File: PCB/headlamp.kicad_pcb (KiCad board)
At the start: 2 copper layers, 50 x 38 mm, 54 parts, among them J1 USB_B_Mini, J2 Conn_02x03_Odd_Even, Q1 Q_NPN_BCE, Q2 Q_NPN_BCE, Q3 Q_NPN_BCE, Q4 Q_NPN_BCE, SW1 SW_Push, SW2 SW_Push, SW3 SW_Push, SW4 SW_Push, U1 TP4056, U2 ATtiny13A-SS, X1 BATT+, X2 BATT-

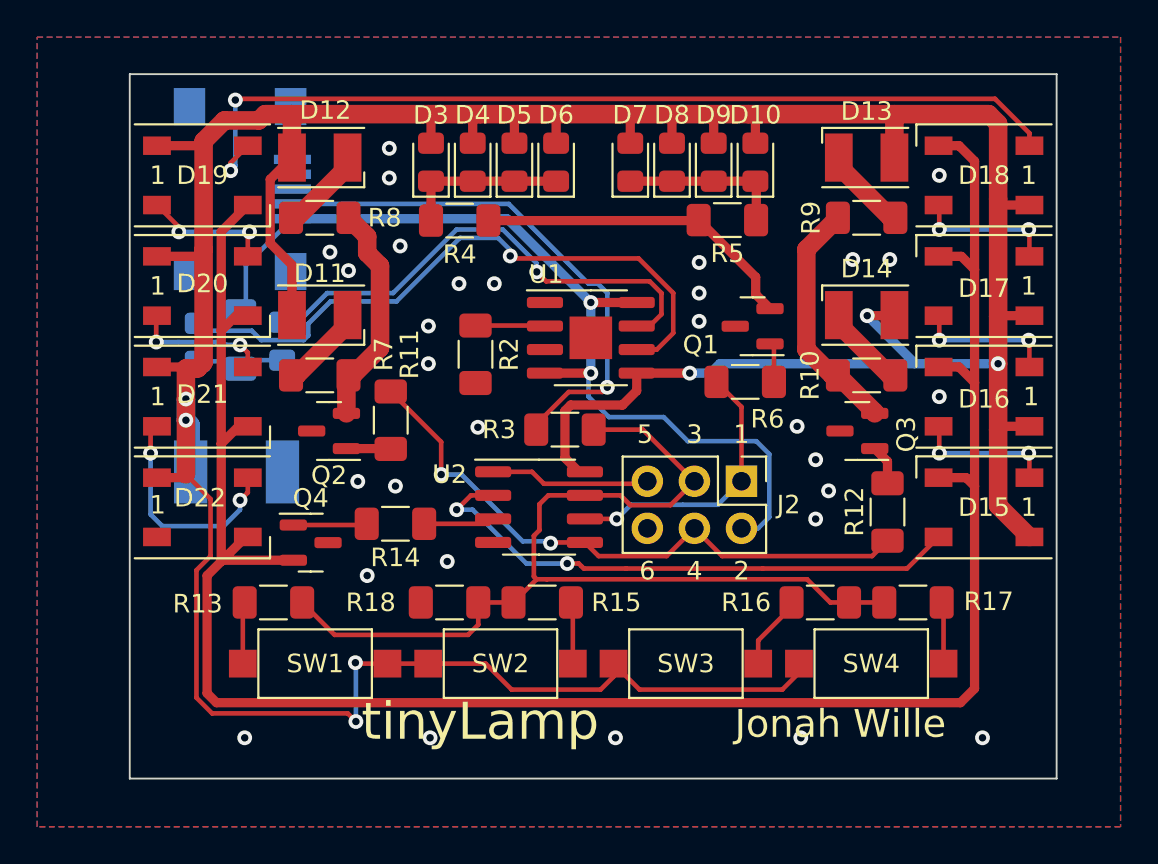
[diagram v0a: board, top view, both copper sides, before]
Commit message: USB con overhang pcb
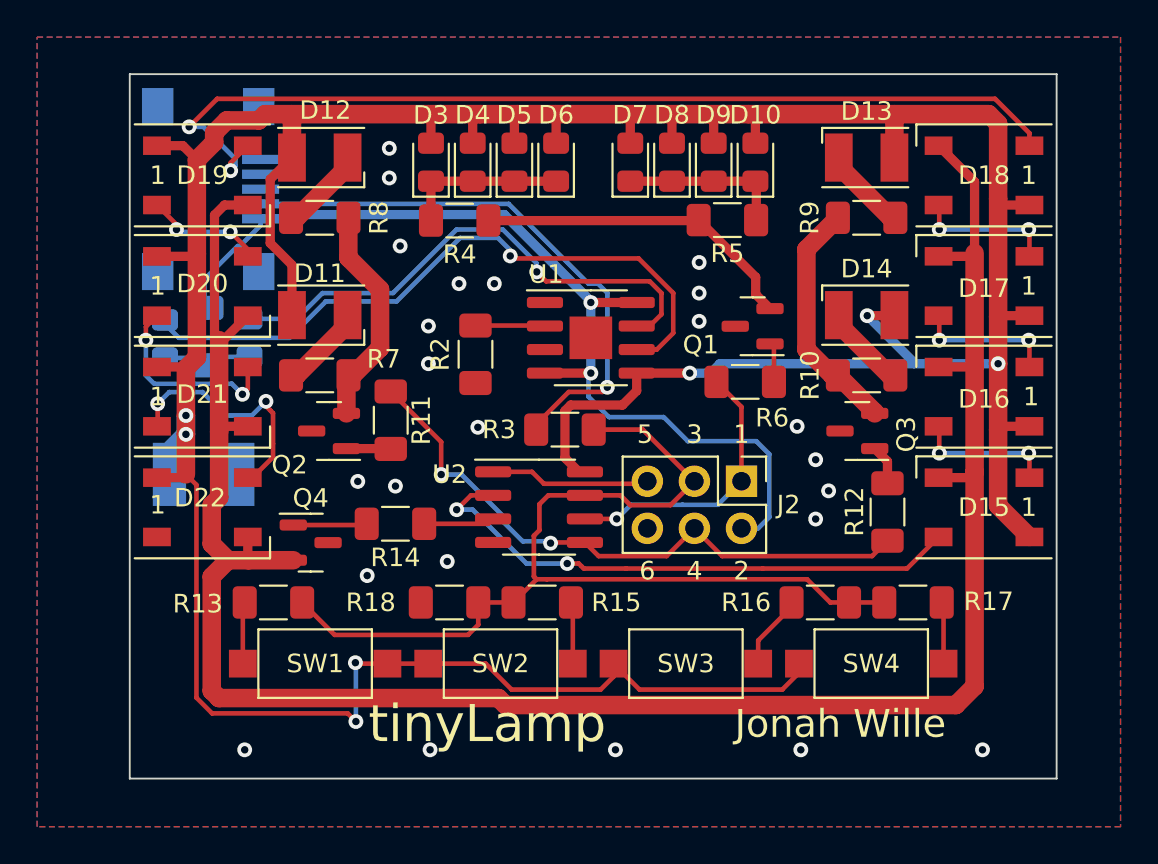
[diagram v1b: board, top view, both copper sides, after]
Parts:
- moved X2 2.42 mm to (-19.2, 13.6)
- moved D1 1.77 mm to (-23.1, 6.29)
- moved D2 1.77 mm to (-18.5, 6.22)
- moved R1 1.77 mm to (-20.8, 6.16)
- moved J1 1.72 mm to (-20.6, -1.80)
- moved X1 1.15 mm to (-22.9, 13.6)
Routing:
- net Net-(D20-Pad2): track 7.39 -> 10.7 mm
- net Net-(D18-Pad2): track 50.0 -> 53.1 mm
- net VCC: track 216.9 -> 214.7 mm
- net VBUS: track 50.4 -> 52.5 mm
- net Net-(J1-Pad2): track 29.0 -> 30.7 mm
- net Net-(D2-Pad1): track 27.0 -> 28.6 mm
- net Net-(D1-Pad1): track 34.6 -> 36.1 mm
- net Net-(D15-Pad3): track 116.1 -> 115.1 mm
- net Net-(D21-Pad2): track 12.2 -> 13.2 mm
- net Net-(D19-Pad2): track 7.11 -> 6.43 mm
- net GND: vias 30 -> 24
